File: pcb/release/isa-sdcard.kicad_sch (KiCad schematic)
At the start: 48 parts, among them J1 Micro_SD_Card_Det1, J2 Bus_ISA_8bit_AB_Rev0, SW1 ADDR SEL, U1 74HC00, U10 74HC74, U11 74HC08, U12 74HC04, U13 74HC74, U16 AMS1117-3.3, U2 74HCT32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

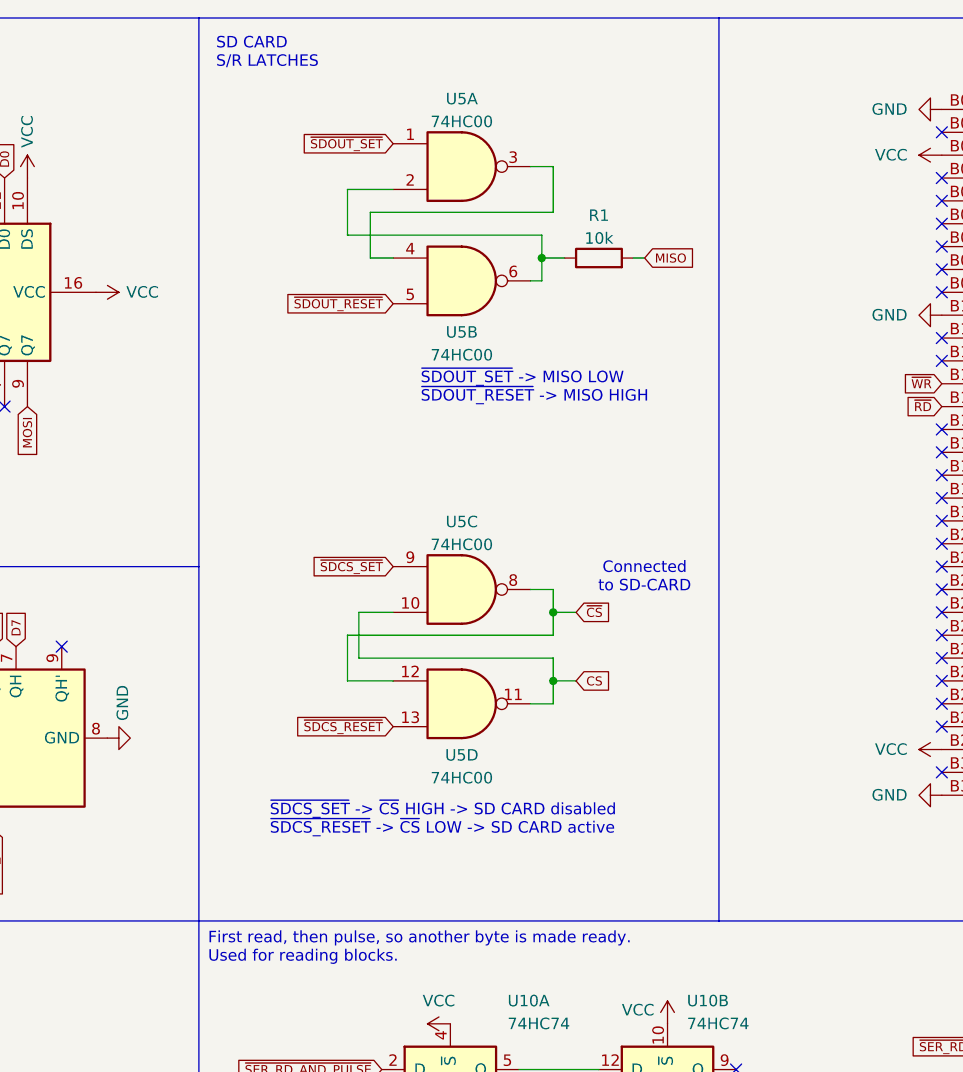
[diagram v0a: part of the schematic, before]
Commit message: Adding delays and improving bracket
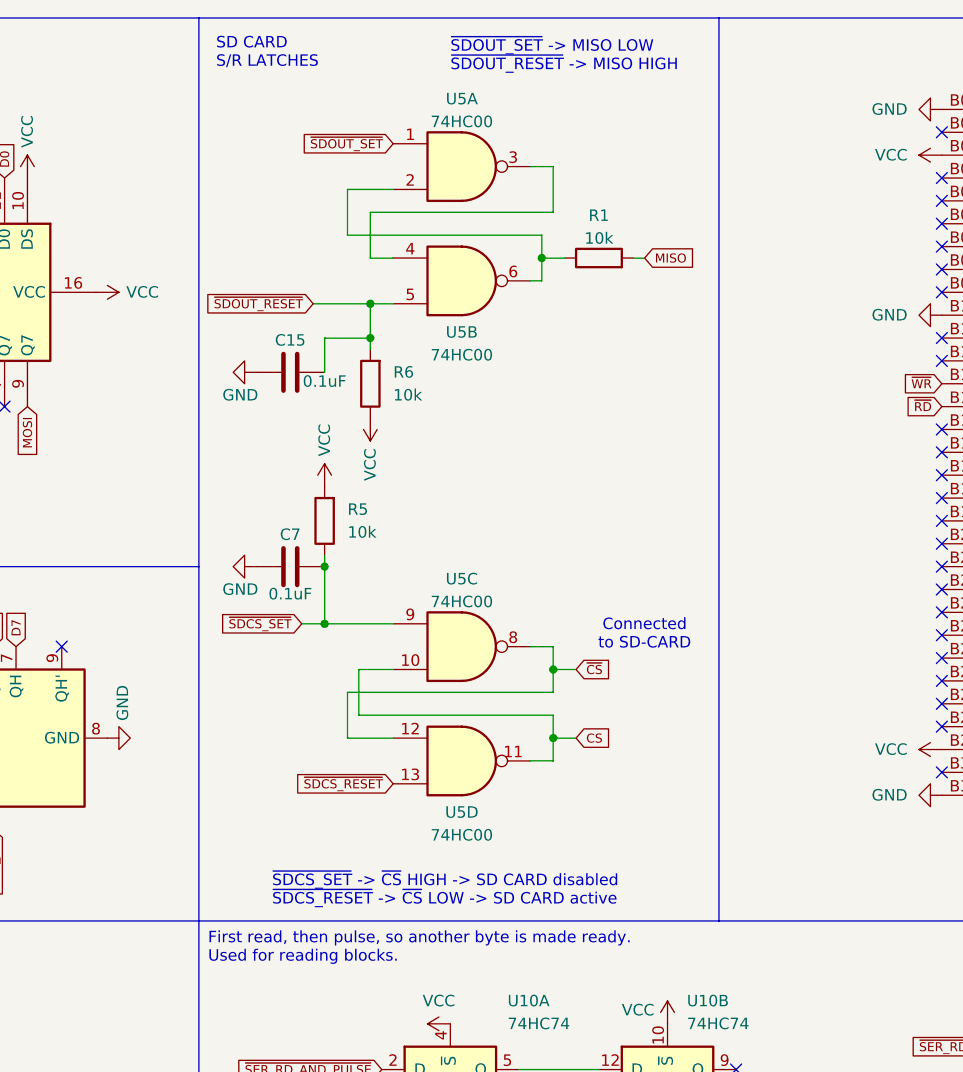
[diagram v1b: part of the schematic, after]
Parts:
- added C15, C7: 0.1uF, Capacitor_SMD:C_0805_2012Metric, symbol Device:C
- added R5, R6: 10k, Resistor_SMD:R_0805_2012Metric, symbol Device:R
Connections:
- net GND: now also C15.2, C7.2
- net VCC: now also R5.2, R6.1
- net ~{SDCS_SET}: now also C7.1, R5.1
- net ~{SDOUT_RESET}: now also C15.1, R6.2
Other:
- moved on the sheet: U5C, U5D
